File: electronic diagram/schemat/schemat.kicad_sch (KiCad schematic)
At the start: 14 parts, among them J1 Conn_01x03_Pin, J2 Conn_01x03_Pin, J3 Conn_01x03_Pin, J4 Conn_01x03_Pin, SW1 SW_Push, U1 ESP32-S3-DevKitC, U2 MPU-6050

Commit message: Aktualna wersja schematu elektronicznego
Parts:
- removed D1, D2, D3, D4: WS2812B, LED_SMD:LED_WS2812B_PLCC4_5.0x5.0mm_P3.2mm, symbol LED:WS2812B
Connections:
- net at A2.15 (STEP): now also U1.5 (GPIO5/ADC1_CH4); no longer U1.4 (GPIO4/ADC1_CH3)
- net at A2.16 (DIR): now also U1.4 (GPIO4/ADC1_CH3); no longer U1.5 (GPIO5/ADC1_CH4)
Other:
- moved on the sheet: U2, U3

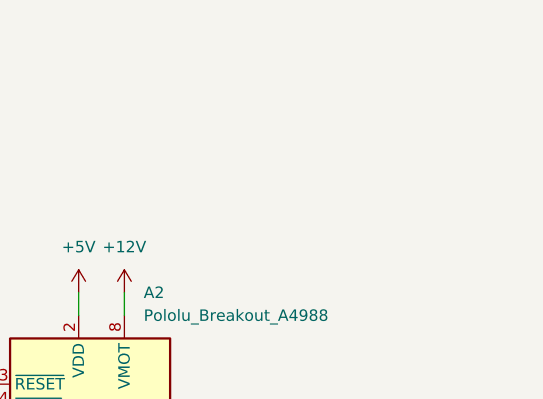
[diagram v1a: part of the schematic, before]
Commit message: Dodanie schematów blokowych oraz dodanie regulatora 5V do schematu
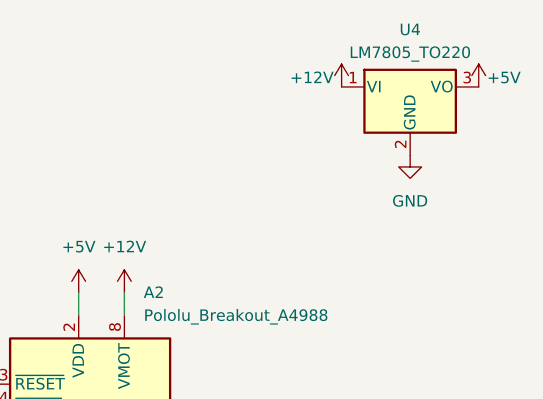
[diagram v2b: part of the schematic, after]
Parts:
- added U4: LM7805_TO220, Package_TO_SOT_THT:TO-220-3_Vertical, symbol Regulator_Linear:LM7805_TO220
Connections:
- net +12V: now also U4.1 (VI)
- net +5V: now also U4.3 (VO)
- net GND: now also U4.2 (GND)
